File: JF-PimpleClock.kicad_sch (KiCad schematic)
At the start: 44 parts, among them J1 Conn_01x06_Female, J2 Conn_01x08_Female, J3 Conn_01x08_Female, SW1 SW_Push, SW2 SW_Push, U1 ATmega328-P, U2 DS3231M, U3 DFPLAYER_MINI, Y1 16 Mhz

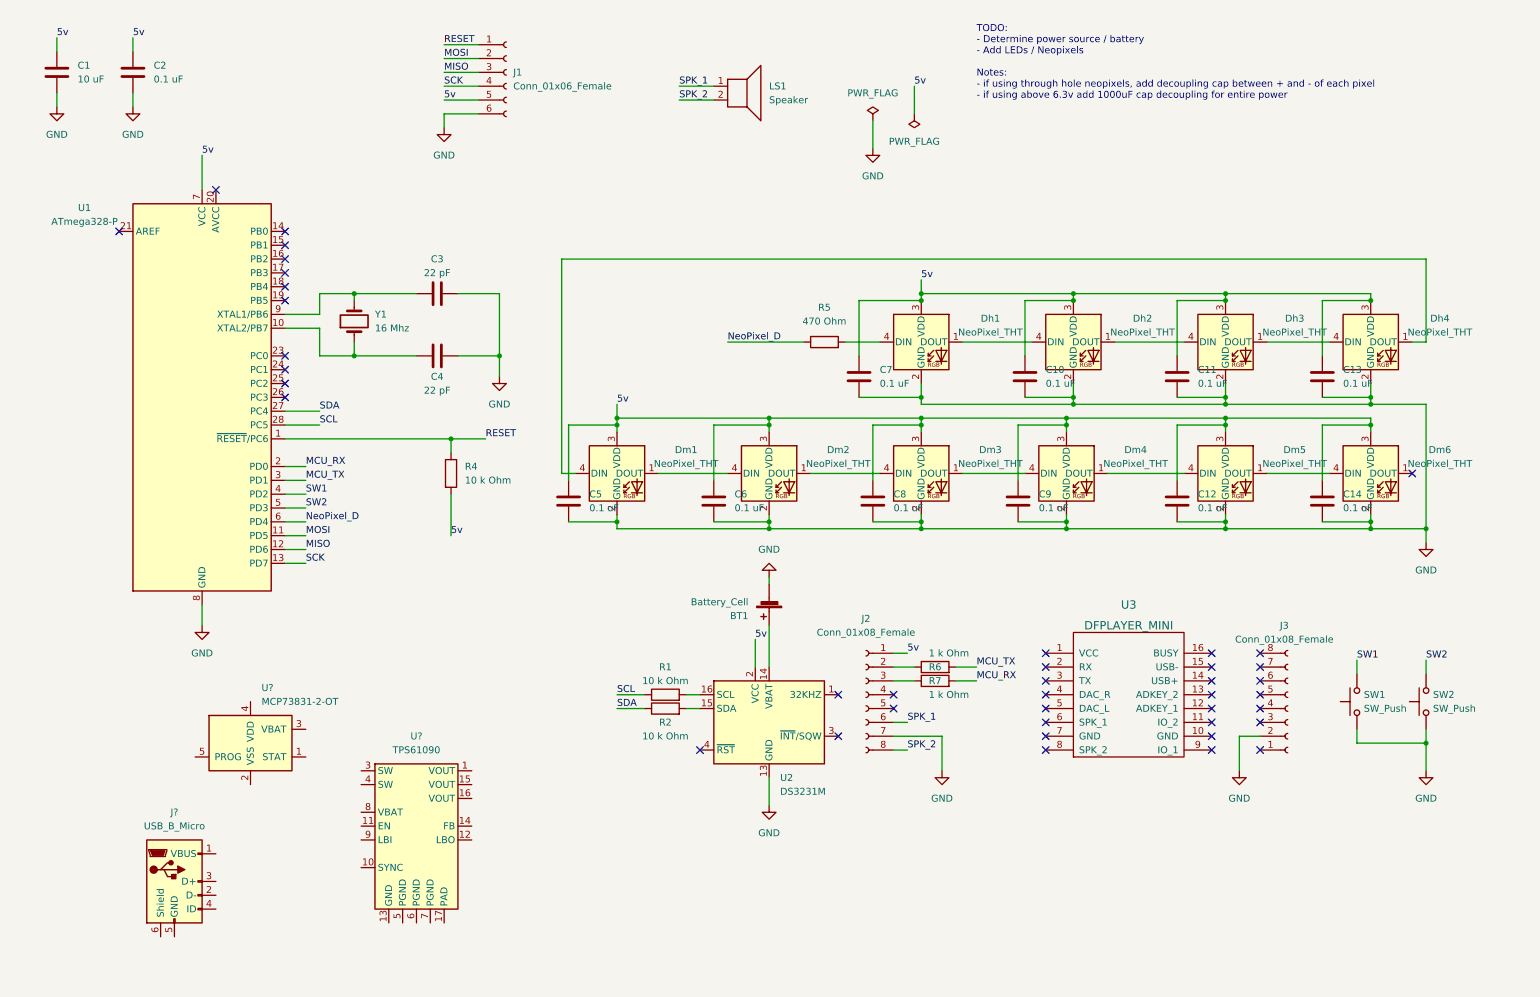
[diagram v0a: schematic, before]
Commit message: init for new voltage regulator and lipo management
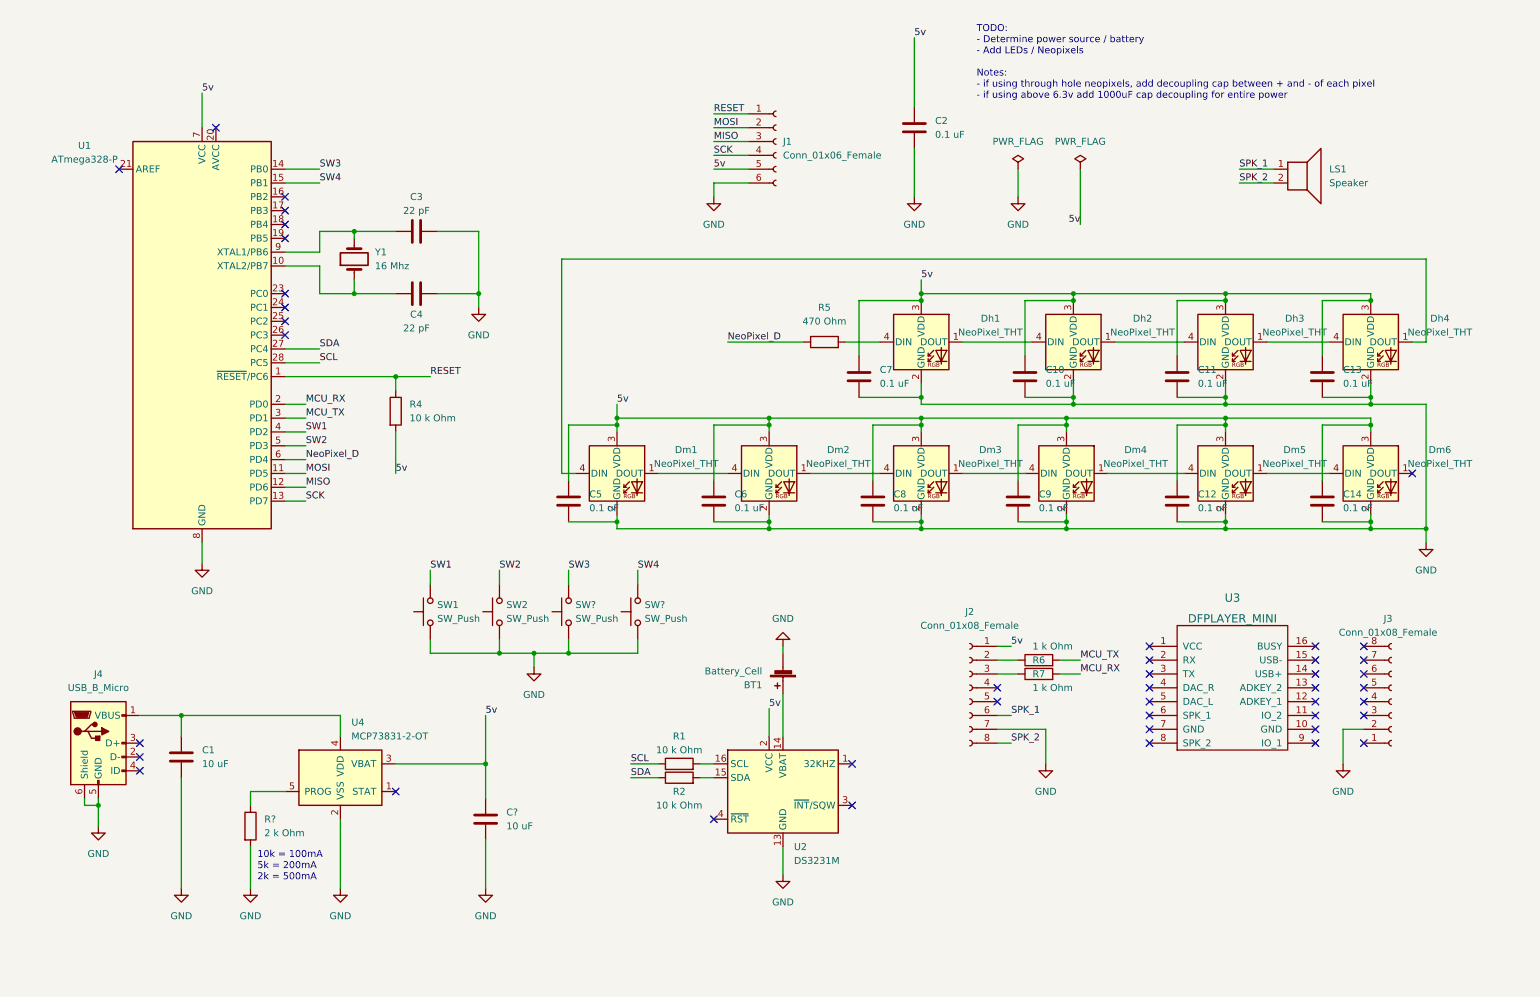
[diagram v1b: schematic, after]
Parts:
- removed U?: TPS61090, Package_DFN_QFN:Texas_S-PVQFN-N16_EP2.7x2.7mm_ThermalVias, symbol Regulator_Switching:TPS61090
- added C?: 10 uF, Capacitor_SMD:C_0805_2012Metric, symbol Device:C
- added R?: 2 k Ohm, symbol Device:R
- added SW? (x2): SW_Push, Button_Switch_SMD:SW_SPST_B3S-1100, symbol Switch:SW_Push
- gave numbers to parts that had none: 2
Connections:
- net 5v: now also U4.3 (VBAT), C?.1; no longer C1.1
- net GND: now also J4.5 (GND), J4.6 (Shield), U4.2 (VSS), C?.2, R?.2, SW?.1, SW?.1
- net at J4.1 (VBUS): now also C1.1, U4.4 (VDD)
- net at U4.5 (PROG): now also R?.1
- net SW3: now reaches U1.14 (PB0)
- net SW3: now also SW?.2
- net SW4: now reaches U1.15 (PB1)
- net SW4: now also SW?.2
- no-connect marks 41 -> 43
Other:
- note added: "10k = 100mA 5k = 200mA 2k = 500mA"
- moved on the sheet: BT1, C1, C2, C3, C4, J1, J2, J3, J4, LS1, R1, R2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

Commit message: init for pcb layout with test outline silk and shape
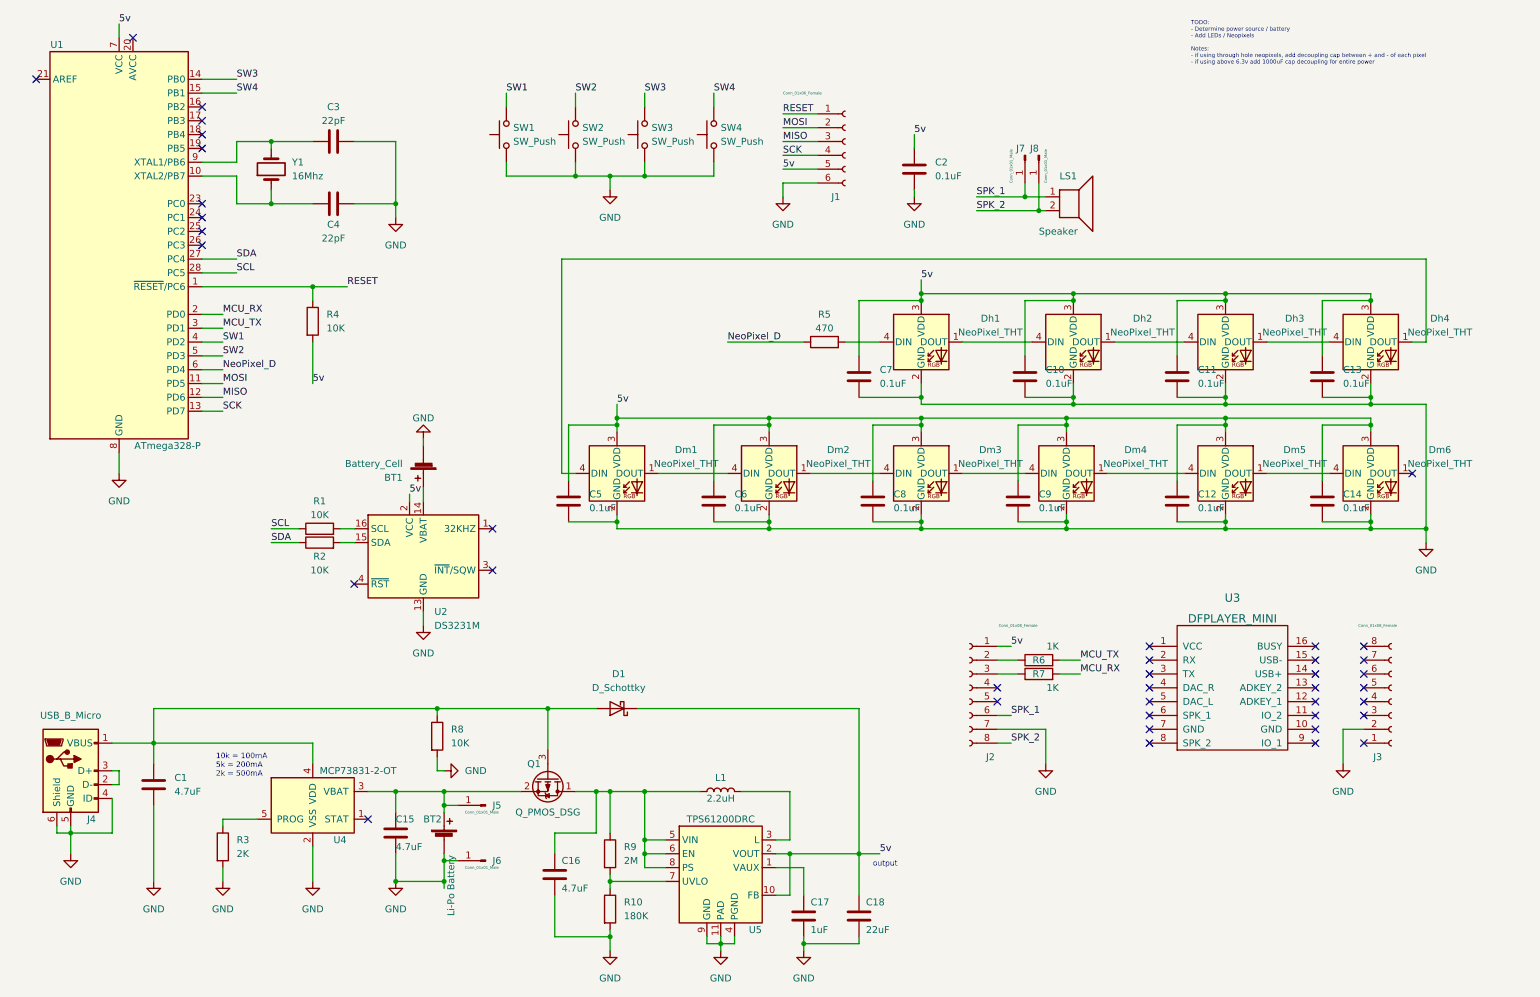
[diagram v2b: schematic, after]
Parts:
- added BT2: Li-Po Battery, symbol Device:Battery_Cell
- added C16: 4.7uF, Capacitor_SMD:C_0805_2012Metric, symbol Device:C
- added C17: 1uF, Capacitor_SMD:C_0805_2012Metric, symbol Device:C
- added C18: 22uF, Capacitor_SMD:C_0805_2012Metric, symbol Device:C
- added D1: D_Schottky, Diode_SMD:D_0402_1005Metric, symbol Device:D_Schottky
- added J5, J6, J7, J8: Conn_01x01_Male, TestPoint:TestPoint_Pad_2.0x2.0mm, symbol Connector:Conn_01x01_Male
- added L1: 2.2uH, Inductor_SMD:L_0603_1608Metric, symbol Device:L
- added Q1: Q_PMOS_DSG, Package_TO_SOT_SMD:TO-263-2, symbol Device:Q_PMOS_DSG
- added R10: 180K, Resistor_SMD:R_0805_2012Metric, symbol Device:R
- added R8: 10K, Resistor_SMD:R_0805_2012Metric, symbol Device:R
- added R9: 2M, Resistor_SMD:R_0805_2012Metric, symbol Device:R
- added U5: TPS61200DRC, Package_SON:Texas_S-PVSON-N10_ThermalVias, symbol Regulator_Switching:TPS61200DRC
- BT1: footprint (none) -> Battery:Battery_Panasonic_CR3032-VCN_Vertical_CircularHoles
- C1: value 10 uF -> 4.7uF
- C10, C11, C12, C13, C14, C2, C5, C6, C7, C8, C9: value 0.1 uF -> 0.1uF
- C15: renamed from C?; value 10 uF -> 4.7uF
- C3, C4: value 22 pF -> 22pF
- J4: footprint (none) -> Connector_USB:USB_Micro-B_Molex-105017-0001
- R1, R2, R4: value 10 k Ohm -> 10K
- R3: renamed from R?; value 2 k Ohm -> 2K; footprint (none) -> Resistor_SMD:R_0805_2012Metric
- R5: value 470 Ohm -> 470
- R6, R7: value 1 k Ohm -> 1K
- Y1: value 16 Mhz -> 16Mhz
- gave numbers to parts that had none: 2
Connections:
- net 5v: now also C18.1, D1.1 (K), U5.10 (FB), U5.2 (VOUT); no longer C15.1, U4.3 (VBAT)
- net GND: now also J4.4 (ID), BT2.2 (-), C16.2, C17.2, C18.2, J6.1 (Pin_1), R10.2, R8.2, U5.11 (PAD), U5.4 (PGND), U5.9 (GND)
- net SPK_1: now also J7.1 (Pin_1)
- net SPK_2: now also J8.1 (Pin_1)
- net at C1.1, J4.1 (VBUS), U4.4 (VDD): now also D1.2 (A), Q1.3 (G), R8.1
- net at J4.2 (D-): now also J4.3 (D+)
- new net: C16.1, L1.1, Q1.1 (D), R9.1, U5.5 (VIN), U5.6 (EN), U5.8 (PS)
- new net: R10.1, R9.2, U5.7 (UVLO)
- new net: BT2.1 (+), C15.1, J5.1 (Pin_1), Q1.2 (S), U4.3 (VBAT)
- new net: L1.2, U5.3 (L)
- new net: C17.1, U5.1 (VAUX)
- no-connect marks 43 -> 40
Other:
- note added: "output"
- moved on the sheet: BT1, C1, C15, C2, C3, C4, J1, J4, LS1, R1, R2, R3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

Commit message: started first pcb test layout and some part assignment to jcl
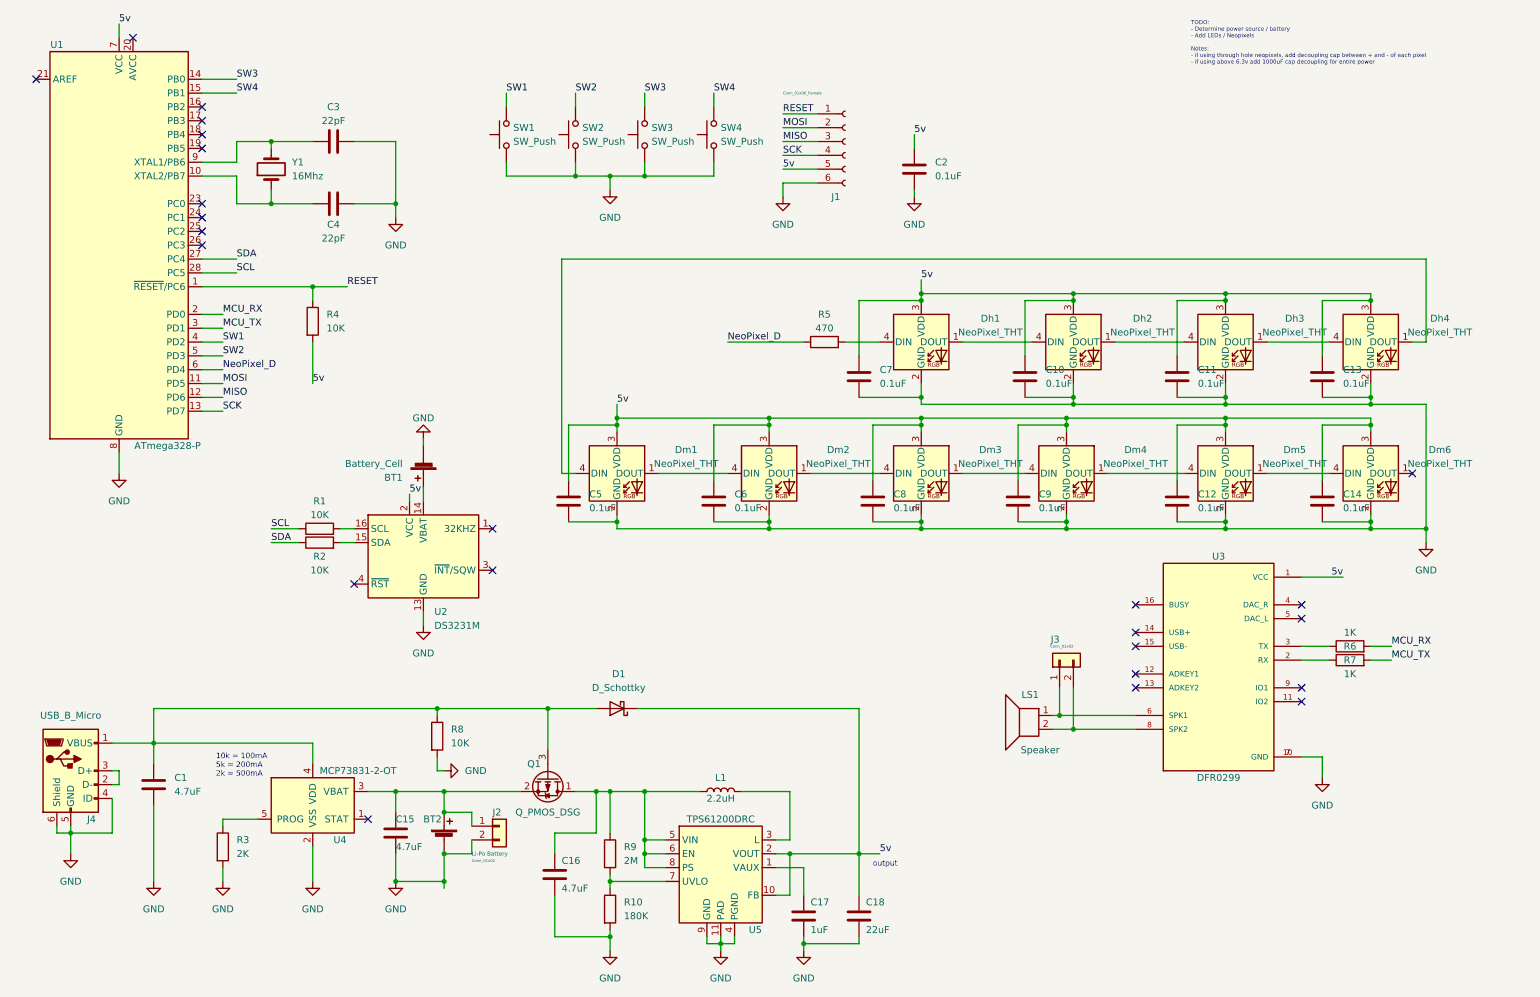
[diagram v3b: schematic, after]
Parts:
- removed J2, J3: Conn_01x08_Female, Connector_PinSocket_2.54mm:PinSocket_1x08_P2.54mm_Horizontal, symbol Connector:Conn_01x08_Female
- removed J5, J6, J7, J8: Conn_01x01_Male, TestPoint:TestPoint_Pad_2.0x2.0mm, symbol Connector:Conn_01x01_Male
- removed U3: DFPLAYER_MINI, symbol Misc_ICs:DFPLAYER_MINI
- added J2: Conn_01x02, Connector_JST:JST_EH_S2B-EH_1x02_P2.50mm_Horizontal, symbol Connector_Generic:Conn_01x02
- added J3: Conn_01x02, TestPoint:TestPoint_2Pads_Pitch2.54mm_Drill0.8mm, symbol Connector_Generic:Conn_01x02
- added U3: DFR0299, Arduino_Nano:DFPlayer_V2, symbol DFR0299:DFR0299
- BT1: footprint Battery:Battery_Panasonic_CR3032-VCN_Vertical_CircularHoles -> Battery:BatteryHolder_Keystone_3002_1x2032
- J1: footprint Connector_PinSocket_2.54mm:PinSocket_1x06_P2.54mm_Horizontal -> Connector_PinHeader_2.54mm:PinHeader_1x06_P2.54mm_Vertical
- Q1: footprint Package_TO_SOT_SMD:TO-263-2 -> Package_TO_SOT_SMD:SOT-23
- Y1: footprint Crystal:Crystal_SMD_7050-2Pin_7.0x5.0mm -> Crystal:Crystal_SMD_2012-2Pin_2.0x1.2mm
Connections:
- net 5v: now also U3.1 (VCC)
- net GND: now also J2.2 (Pin_2), U3.10 (GND), U3.7 (GND)
- net MCU_RX: now also R6.2; no longer R7.2
- net MCU_TX: now also R7.2; no longer R6.2
- net at BT2.1 (+), C15.1, Q1.2 (S)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: now also J2.1 (Pin_1)
- net at R7.1: now also U3.2 (RX)
- net at R6.1: now also U3.3 (TX)
- net SPK_1: no longer names the net of LS1.1
- net SPK_1: now also J3.1 (Pin_1), U3.6 (SPK1)
- net SPK_2: no longer names the net of LS1.2
- net SPK_2: now also J3.2 (Pin_2), U3.8 (SPK2)
- no-connect marks 40 -> 24
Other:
- moved on the sheet: LS1

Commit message: update pcb layout, swapped a few parts to make them easier for assembly
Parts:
- BT1: footprint Battery:BatteryHolder_Keystone_3002_1x2032 -> Battery:BatteryHolder_Keystone_1060_1x2032
- Y1: footprint Crystal:Crystal_SMD_2012-2Pin_2.0x1.2mm -> Crystal:Crystal_SMD_HC49-SD
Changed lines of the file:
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@@
       (effects (font (size 1.27 1.27)) (justify right))
     )
-    (property "Footprint" "Crystal:Crystal_SMD_2012-2Pin_2.0x1.2mm" (id 2) (at 60.96 43.18 0)
+    (property "Footprint" "Crystal:Crystal_SMD_HC49-SD" (id 2) (at 60.96 43.18 0)
       (effects (font (size 1.27 1.27)) hide)
     )
@@
       (effects (font (size 1.27 1.27)) (justify left))
     )
-    (property "Footprint" "Battery:BatteryHolder_Keystone_3002_1x2032" (id 2) (at 88.9 98.044 90)
+    (property "Footprint" "Battery:BatteryHolder_Keystone_1060_1x2032" (id 2) (at 88.9 98.044 90)
       (effects (font (size 1.27 1.27)) hide)
     )
@@
     )
     (path "/f58a2942-2c03-48af-bf7b-010ef19383bc"
-      (reference "BT1") (unit 1) (value "Battery_Cell") (footprint "Battery:BatteryHolder_Keystone_3002_1x2032")
+      (reference "BT1") (unit 1) (value "Battery_Cell") (footprint "Battery:BatteryHolder_Keystone_1060_1x2032")
     )
     (path "/e35f40bf-e2f4-4983-a837-faf26800d84f"
@@
     )
     (path "/ba7aaaa8-9f4f-4fb9-b3c5-6e0d28dc1372"
-      (reference "Y1") (unit 1) (value "16Mhz") (footprint "Crystal:Crystal_SMD_2012-2Pin_2.0x1.2mm")
-    )
-  )
+      (reference "Y1") (unit 1) (value "16Mhz") (footprint "Crystal:Crystal_SMD_HC49-SD")
+    )
+  )
